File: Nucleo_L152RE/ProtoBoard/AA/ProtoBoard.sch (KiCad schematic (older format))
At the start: 115 parts, among them CON1 USB-MICRO-B, J1 EXT1, J2 EXT2, J3 EXTPower, P1 Power, P10 OW2_A, P11 GND1, P12 I2C1_B, P13 I2C2_B, P14 SW_1_6, P15 WS1, P16 WS2, P17 MS2, P18 WS3, P19 WS4, P2 VinPower, P20 GND2, P21 Hole, P22 MS3, P23 OW3_A, P24 OW4_A, P25 MS4, P26 Hole, P27 Hole, P28 RGB1, P29 Ant, P3 USART2, P30 Hole, P4 SWD Header, P5 USART1, P6 MS1, P7 I2C1_A, P8 I2C2_A, P9 OW1_A, Q1 SI2323DS, SW1 MomentarySwitch, U2 Nucleo-L152RE-CN7, U3 Nucleo-L152RE-CN10, U5 MT3329_GPS, U6 S25FL127S, U7 RFM69HW

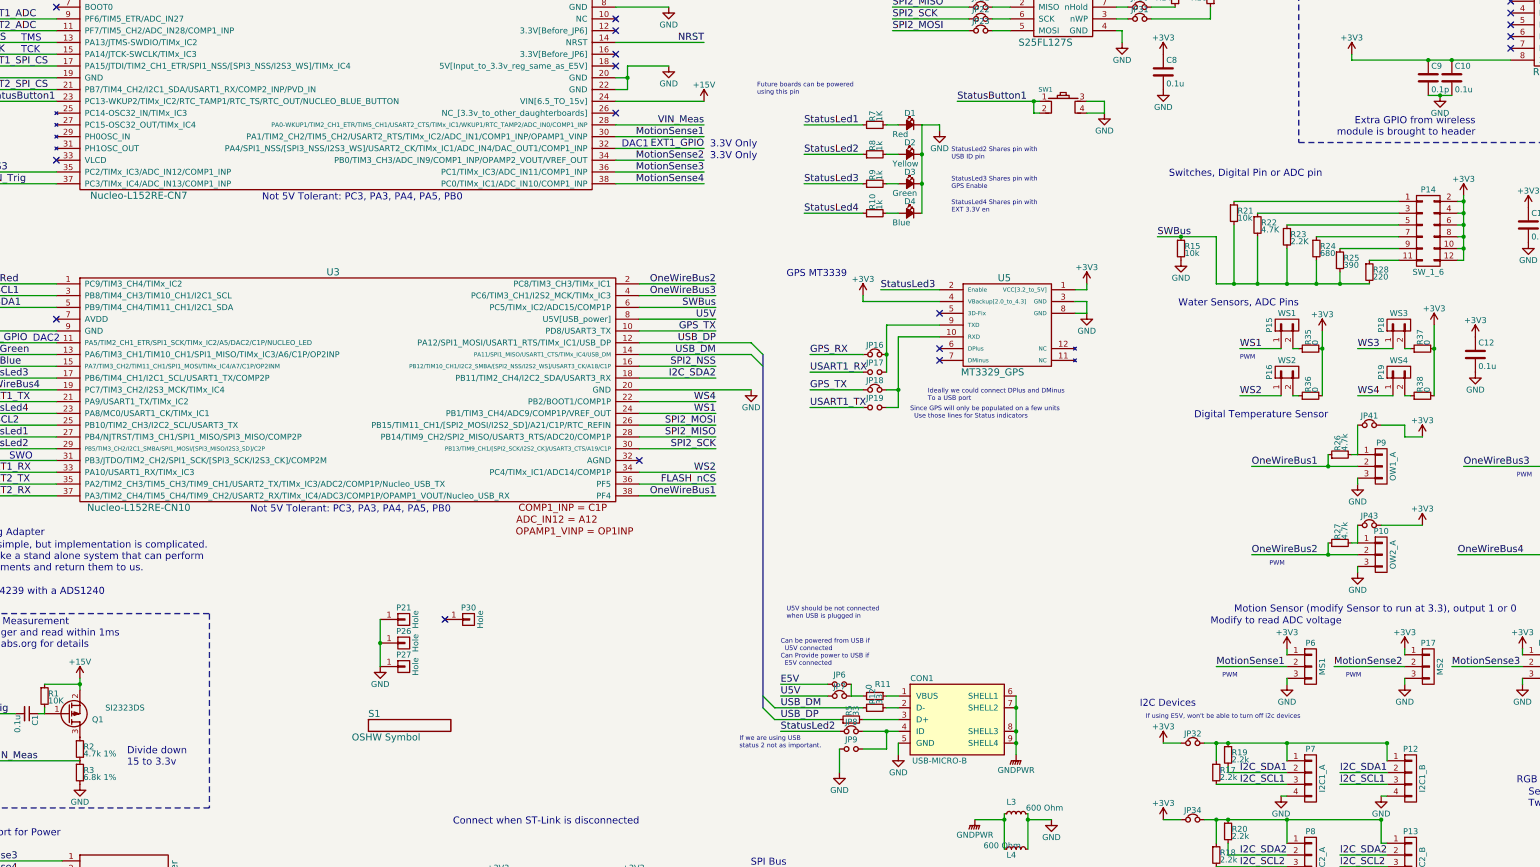
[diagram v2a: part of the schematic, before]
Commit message: Updated schematic with links to almost all parts.
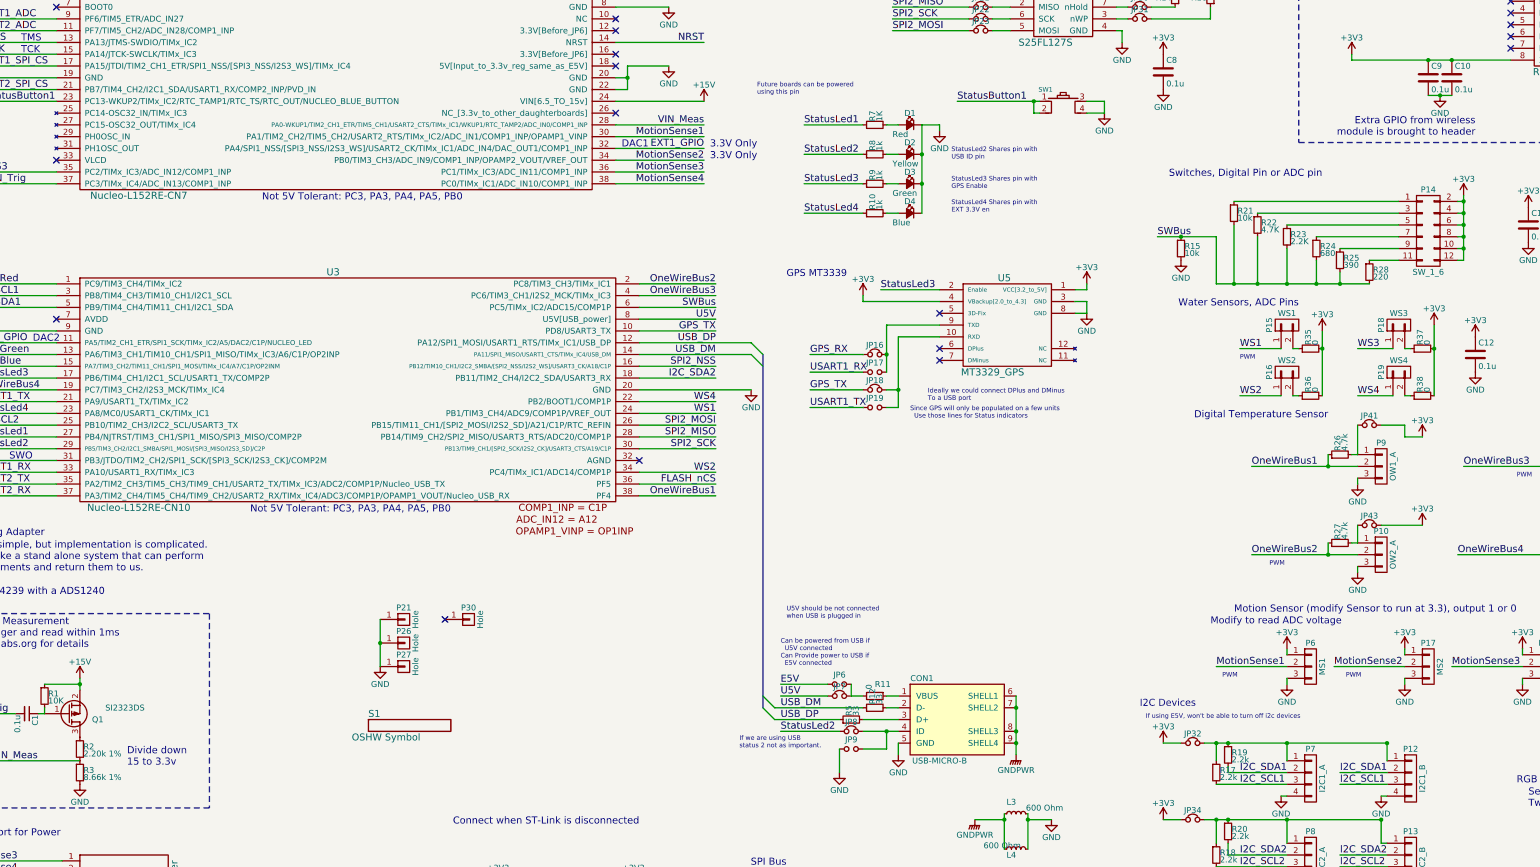
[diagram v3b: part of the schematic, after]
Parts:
- C1, C10, C11, C12, C8: Digikey Part Number (none) -> 490-1532-1-ND
- C9: value 0.1p -> 0.1u; Digikey Part Number (none) -> 490-1532-1-ND
- Q1: Digikey Part Number (none) -> SI2323DS-T1-E3CT-ND
- R1, R15, R21, R39: Digikey Part Number (none) -> P10KGCT-ND; Digikey URL (none) -> http://www.digikey.com/product-detail/en/ERJ-3GEYJ103V/P10K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
- R10, R7, R8, R9: Digikey Part Number (none) -> P1.0KGCT-ND
- R11: Digikey Part Number (none) -> P0.0HCT-ND
- R12, R5: Digikey Part Number (none) -> P33HCT-ND
- R13, R35, R36, R37, R38, R6: Digikey Part Number (none) -> P0.0GCT-ND
- R14: Digikey Part Number (none) -> RMCF0603FT100KTR-ND
- R16: Digikey Part Number (none) -> RMCF0603FT100KTR-ND; Digikey URL (none) -> http://www.digikey.com/product-detail/en/RMCF0603FT100K/RMC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
- R17, R18, R19, R20, R23: Digikey Part Number (none) -> P2.2KGCT-ND
- R2: value 4.7k 1% -> 2.20k 1%; Digikey Part Number (none) -> P2.20KHCT-ND
- R22, R40: Digikey Part Number (none) -> P4.7KGCT-ND; Digikey URL (none) -> http://www.digikey.com/product-detail/en/ERJ-3GEYJ472V/P4.7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
- R24: Digikey Part Number (none) -> P680GCT-ND
- R25: Digikey Part Number (none) -> P390GCT-ND
- R26, R27, R41: Digikey Part Number (none) -> P4.7KGCT-ND
- R28, R42, R43, R44: Digikey Part Number (none) -> P220GCT-ND
- R3: value 6.8k 1% -> 8.66k 1%; Digikey Part Number (none) -> P8.66KHCT-ND
- U2: Digikey Part Number (none) -> 497-14363-ND
- U3: Ebay (none) -> 40 2.54 female round header pin
- U7: Ebay (none) -> RFM69HW 915MHz

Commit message: Ordered parts from Mouser for Protoboard AA.
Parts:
- C1, C10, C11, C12, C8, C9: MFG (none) -> GRM188R71C104KA01D
- CON1: MFG (none) -> 10104111-0001LF
- D1: MFG (none) -> LTST-C191KRKT
- D2: MFG (none) -> LTST-C191KSKT
- D3: MFG (none) -> LTST-C191KGKT
- D4: MFG (none) -> LTST-C191TBKT
- J1, J2, J3: MFG (none) -> RJLSE4238101T
- L3, L4: MFG (none) -> MI0603J601R-10
- Q1: MFG (none) -> SI2323DS-T1-E3
- R1, R15, R21, R39: MFG (none) -> ERJ-3GEYJ103V
- R10, R7, R8: MFG (none) -> ERJ-3GEYJ102V
- R11, R13, R35, R36, R37, R38, R6: MFG (none) -> ERJ-3GEY0R00V
- R12, R5: MFG (none) -> ERJ-3EKF33R0V
- R14, R16: MFG (none) -> CRCW0603100KFKEA
- R17, R18, R19, R20, R23, R42, R43, R44: MFG (none) -> ERJ-3GEYJ222V
- R2: MFG (none) -> ERJ-3EKF2201V
- R22, R26, R27, R40, R41: MFG (none) -> ERJ-3GEYJ472V
- R24: MFG (none) -> CRCW0603680RFKEA
- R25: MFG (none) -> ERJ-3GEYJ390V
- R28: MFG (none) -> ERJ-3GEYJ220V
- R3: MFG (none) -> ERJ-3EKF8661V
- SW1: MFG (none) -> 1825910-6
- U2: MFG (none) -> NUCLEO-L152RE
- U6: Digikey Part Number SI2323DS-T1-E3CT-ND -> 1274-1045-ND; Digikey URL http://www.digikey.com/product-detail/en/SI2323DS-T1-E3/SI2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 -> http://www.digikey.com/product-detail/en/S25FL127SABMFI101/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; MFG (none) -> S25FL127SABMFI101

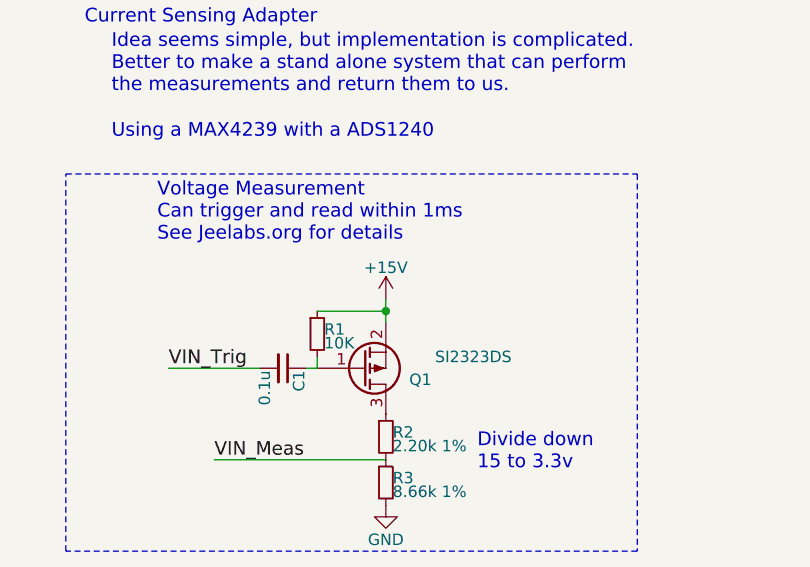
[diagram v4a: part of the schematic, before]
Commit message: Submitted first printing of AA version. Uploading Gerbers since we would like to be able to get back to this point.
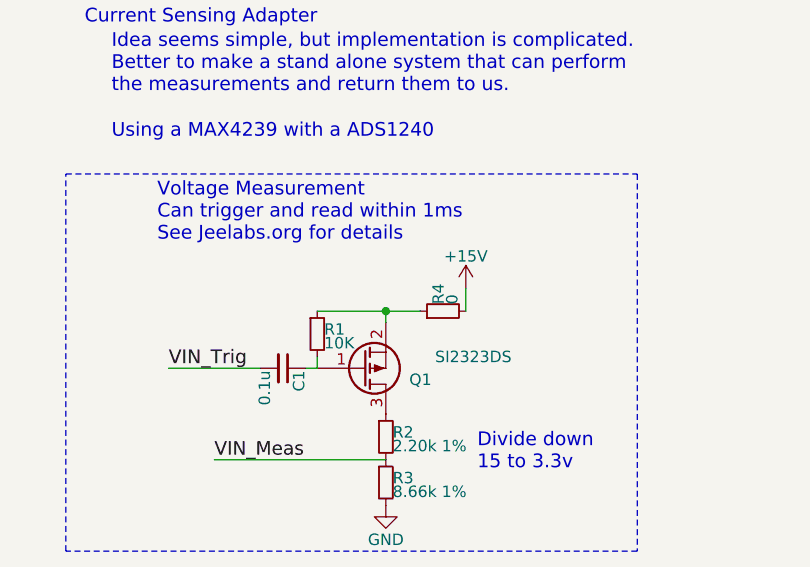
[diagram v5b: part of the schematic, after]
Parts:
- added R4: 0, Resistors_SMD:R_0603_HandSoldering, symbol R_Small
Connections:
- net +15V: now also R4.2; no longer Q1.2 (S), R1.1
- new net: Q1.2 (S), R1.1, R4.1
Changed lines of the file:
@@
 	1600 7450 1600 7500
 Wire Wire Line
-	1600 7250 1900 7250
-Connection ~ 1900 7250
+	1600 7250 2050 7250
 Wire Wire Line
 	1900 7900 1150 7900
@@
 L +15V #PWR073
 U 1 1 5527FBCF
-P 1900 7200
-F 0 "#PWR073" H 1900 7050 50  0001 C CNN
-F 1 "+15V" H 1900 7340 50  0000 C CNN
-F 2 "" H 1900 7200 60  0000 C CNN
-F 3 "" H 1900 7200 60  0000 C CNN
-	1    1900 7200
+P 2250 7150
+F 0 "#PWR073" H 2250 7000 50  0001 C CNN
+F 1 "+15V" H 2250 7290 50  0000 C CNN
+F 2 "" H 2250 7150 60  0000 C CNN
+F 3 "" H 2250 7150 60  0000 C CNN
+	1    2250 7150
 	1    0    0    -1
 $EndComp
@@
 	1    0    0    -1
 $EndComp
-Wire Wire Line
-	1900 7200 1900 7300
 Text Notes 550  800  0    60   ~ 0
 KICAD won't find unconnected nets\n
@@
 	1    0    0    -1
 $EndComp
+$Comp
+L R_Small R4
+U 1 1 55284A56
+P 2150 7250
+F 0 "R4" H 2180 7270 50  0000 L CNN
+F 1 "0" H 2180 7210 50  0000 L CNN
+F 2 "Resistors_SMD:R_0603_HandSoldering" H 2150 7250 60  0001 C CNN
+F 3 "" H 2150 7250 60  0000 C CNN
+F 4 "P0.0GCT-ND" H 2150 7250 60  0001 C CNN "Digikey Part Number"
+F 5 "ERJ-3GEY0R00V" H 1800 -400 60  0001 C CNN "MFG"
+	1    2150 7250
+	0    -1   -1   0
+$EndComp
+Wire Wire Line
+	2250 7150 2250 7250
+Wire Wire Line
+	1900 7250 1900 7300
+Connection ~ 1900 7250
 $EndSCHEMATC
